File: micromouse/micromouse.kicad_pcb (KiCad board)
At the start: 2 copper layers, 38 parts, among them IC1 STM32F205RET7, J1 B2B-PH-K-S, J2 B2B-PH-K-S, J3 Left Header, J4 Left Header, Q1 SFH_313_FA-3_4, SW1 CK_KMS2xxG, U2 AZ1117IH-3.3TRG1, U3 L293DD, U4 BS170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

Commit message: subsystem grouping
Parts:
- added LED2: LTST-C194TBKT, blue-led:LEDC1608X35N, F.Cu at (92.8, 133.9)
- added LED3: LTST-C194TBKT, blue-led:LEDC1608X35N, F.Cu at (90.8, 64.2)
- added R7: 100 ohm, Resistor_SMD:R_0805_2012Metric, F.Cu at (89.2, 134.1)
- moved J3 116.2 mm to (109.3, 103.2), turned to -90 degrees
- moved C76 114.6 mm to (135.8, 12.5)
- moved C75 111.6 mm to (135.8, 15.3), turned to 180 degrees
- moved J4 110.4 mm to (105.2, 103.2), turned to -90 degrees
- moved U4 108.6 mm to (79.2, 138.4), turned to -90 degrees
- moved C9 106.7 mm to (134.2, 26.8), turned to -90 degrees
- moved C77 105.7 mm to (120.3, 9.45)
- moved C72 103.2 mm to (123.1, 26.8), turned to 180 degrees
- moved C73 99.4 mm to (130.8, 26.6), turned to -90 degrees
- moved R5 99.2 mm to (124.8, 8.06), turned to -90 degrees
- moved C70 98.3 mm to (117.6, 21.2), turned to -90 degrees
- moved LED1 98.2 mm to (79.6, 132.6), turned to 90 degrees
- moved C71 97.5 mm to (114.6, 21.2), turned to -90 degrees
- moved C25 97.0 mm to (123.0, 31.2), turned to 180 degrees
- moved C74 95.1 mm to (117.7, 14.4), turned to 180 degrees
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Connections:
- C5 pad 2: unconnected-(C5-Pad2) -> GND
- R4 pad 2: GND -> Net-(LED3-A)

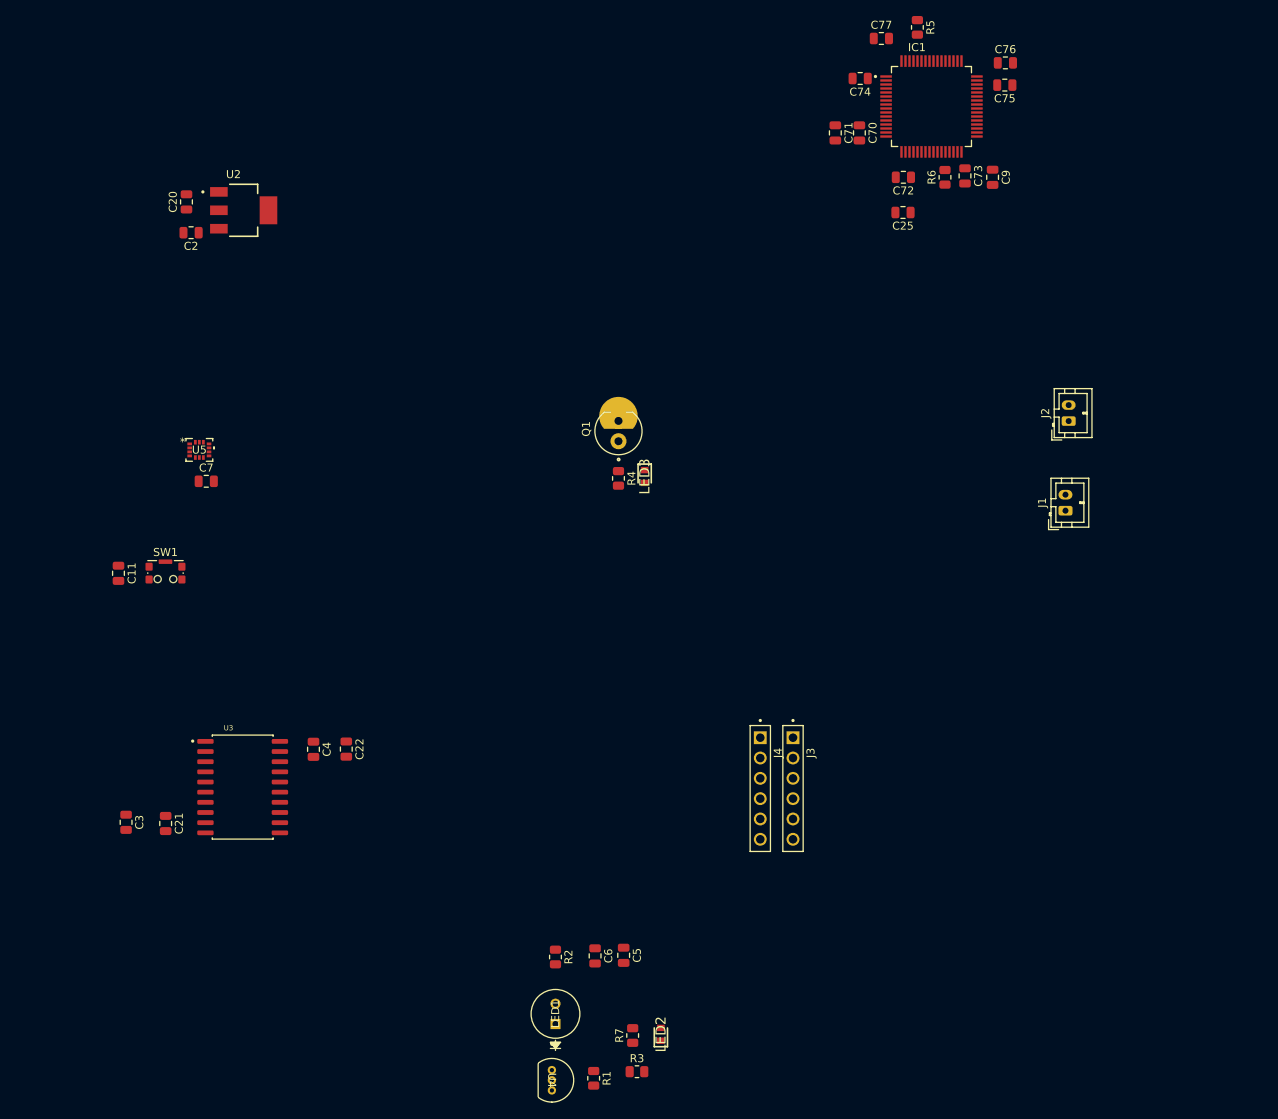
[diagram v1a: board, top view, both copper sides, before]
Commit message: Revision + adding motors
changes to schematic and pcb layout
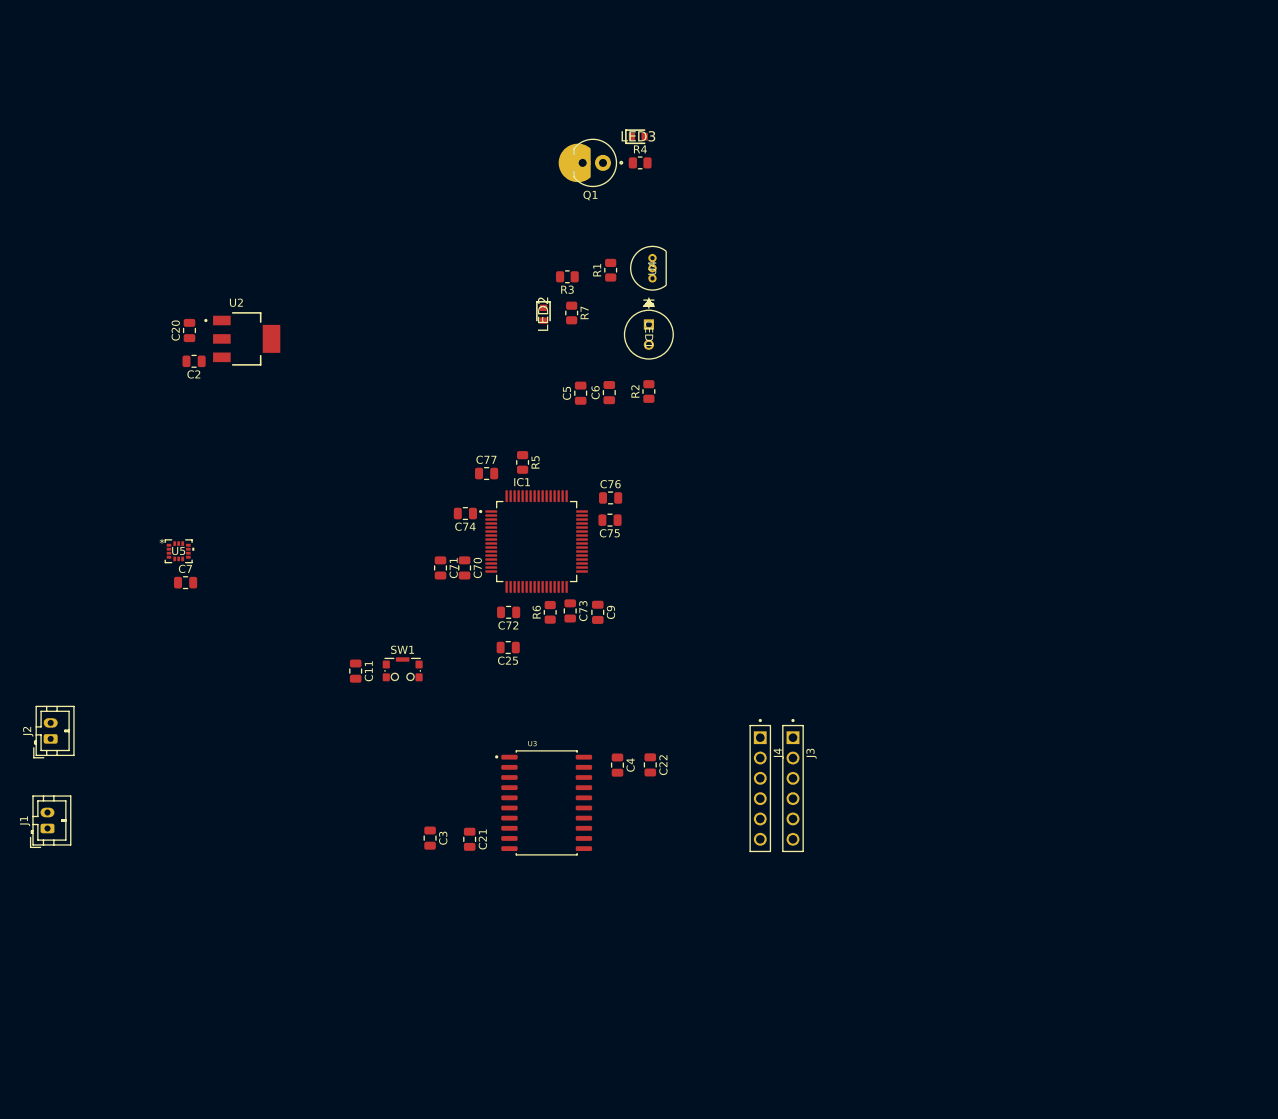
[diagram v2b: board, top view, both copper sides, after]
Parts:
- moved J1 133.3 mm to (16.1, 108.2)
- moved J2 133.3 mm to (16.5, 97.0)
- moved R1 101.0 mm to (86.5, 38.4), turned to 90 degrees
- moved U4 99.8 mm to (91.7, 39.4), turned to 90 degrees
- moved R3 99.7 mm to (81.1, 39.2), turned to 180 degrees
- moved LED2 91.2 mm to (78.1, 43.9), turned to -90 degrees
- moved R7 90.6 mm to (81.6, 43.8), turned to -90 degrees
- moved LED1 88.2 mm to (91.3, 45.2), turned to -90 degrees
- moved C25 73.4 mm to (73.7, 85.6)
- moved C70 73.4 mm to (68.2, 75.6)
- moved C72 73.4 mm to (73.7, 81.2)
- moved C76 73.4 mm to (86.5, 66.9)
- moved C77 73.4 mm to (71.0, 63.8)
- moved C9 73.4 mm to (84.9, 81.2)
- moved R5 73.4 mm to (75.5, 62.4)
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
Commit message: updates to layout
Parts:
- added C1: 4.7 uF, Capacitor_SMD:C_0805_2012Metric, F.Cu at (119.1, 16.7)
- added C10: 4.7 uF, Capacitor_SMD:C_0805_2012Metric, F.Cu at (62.2, 35.7)
- added C12: 0.1 uF, Capacitor_SMD:C_0805_2012Metric, F.Cu at (59.2, 35.7)
- added C13: 4.7 uF, Capacitor_SMD:C_0805_2012Metric, F.Cu at (144.4, 32.5)
- added C14: 0.1 uF, Capacitor_SMD:C_0805_2012Metric, F.Cu at (141.4, 32.5)
- added C8: 0.1 uF, Capacitor_SMD:C_0805_2012Metric, F.Cu at (115.5, 16.8)
- added LED10: LTST-C194TBKT, blue-led:LEDC1608X35N, F.Cu at (147.0, 51.5)
- added LED11: INL-5AMIR15, ir-emitter:LED_INL-5AMIR15_INO, F.Cu at (159.7, 39.4)
- added LED12: LTST-C194TBKT, blue-led:LEDC1608X35N, F.Cu at (145.2, 39.4)
- added LED4: LTST-C194TBKT, blue-led:LEDC1608X35N, F.Cu at (125.5, 41.1)
- added LED5: INL-5AMIR15, ir-emitter:LED_INL-5AMIR15_INO, F.Cu at (132.5, 22.5)
- added LED6: LTST-C194TBKT, blue-led:LEDC1608X35N, F.Cu at (119.7, 25.5)
- added LED7: LTST-C194TBKT, blue-led:LEDC1608X35N, F.Cu at (48.7, 58.6)
- added LED8: INL-5AMIR15, ir-emitter:LED_INL-5AMIR15_INO, F.Cu at (43.9, 40.4)
- added LED9: LTST-C194TBKT, blue-led:LEDC1608X35N, F.Cu at (59.0, 42.4)
- added Motor1: ~, Pololu_Motor:Pololu_Motor, F.Cu at (48.6, 78.6)
- added Motor2: ~, Pololu_Motor:Pololu_Motor, F.Cu at (155.0, 82.2)
- added Q2: SFH_313_FA-3_4, ir reciever:XDCR_SFH_313_FA-3_4, F.Cu at (123.8, 17.5)
- added Q3: SFH_313_FA-3_4, ir reciever:XDCR_SFH_313_FA-3_4, F.Cu at (51.8, 34.6)
- added Q4: SFH_313_FA-3_4, ir reciever:XDCR_SFH_313_FA-3_4, F.Cu at (151.6, 32.7)
- added R10: 47k, Resistor_SMD:R_0805_2012Metric, F.Cu at (133.2, 34.6)
- added R11: 51 ohm, Resistor_SMD:R_0805_2012Metric, F.Cu at (132.3, 14.4)
- added R12: 1.8k, Resistor_SMD:R_0805_2012Metric, F.Cu at (123.9, 25.7)
- added R13: 300 ohm, Resistor_SMD:R_0805_2012Metric, F.Cu at (48.7, 54.7)
- added R14: 100 ohm, Resistor_SMD:R_0805_2012Metric, F.Cu at (45.4, 53.1)
- added R15: 47k, Resistor_SMD:R_0805_2012Metric, F.Cu at (43.0, 53.3)
- added R16: 51 ohm, Resistor_SMD:R_0805_2012Metric, F.Cu at (43.5, 31.5)
- added R17: 1.8k, Resistor_SMD:R_0805_2012Metric, F.Cu at (53.9, 42.5)
- added R18: 300 ohm, Resistor_SMD:R_0805_2012Metric, F.Cu at (147.0, 46.2)
- added R19: 100 ohm, Resistor_SMD:R_0805_2012Metric, F.Cu at (151.1, 46.5)
- added R20: 47k, Resistor_SMD:R_0805_2012Metric, F.Cu at (161.7, 51.8)
- added R21: 51 ohm, Resistor_SMD:R_0805_2012Metric, F.Cu at (151.9, 25.4)
- added R22: 1.8k, Resistor_SMD:R_0805_2012Metric, F.Cu at (149.9, 39.4)
- added R8: 300 ohm, Resistor_SMD:R_0805_2012Metric, F.Cu at (125.3, 36.4)
- added R9: 100 ohm, Resistor_SMD:R_0805_2012Metric, F.Cu at (129.4, 34.8)
- added SW2: EG1218, power-switch:SW_1218_EWI, F.Cu at (106.7, 109.9)
- added U1: BS170, bs170:TO_SA06_ONS, F.Cu at (131.0, 29.7)
- added U6: BS170, bs170:TO_SA06_ONS, F.Cu at (42.0, 46.9)
- added U7: BS170, bs170:TO_SA06_ONS, F.Cu at (158.4, 46.7)
- R7: value 100 ohm -> 300 ohm
- moved J1 94.4 mm to (110.0, 118.8), turned to 180 degrees
- moved J2 85.0 mm to (98.8, 118.4), turned to 180 degrees
- moved C7 84.7 mm to (108.7, 38.8), turned to 180 degrees
- moved U2 81.2 mm to (104.0, 98.3)
- moved C2 81.1 mm to (94.8, 104.0)
- moved U5 80.4 mm to (104.8, 38.3)
- moved C20 78.5 mm to (93.2, 97.3)
- moved C11 43.9 mm to (73.8, 49.1)
- moved SW1 43.9 mm to (79.7, 49.1)
- moved R2 41.9 mm to (72.1, 16.4), turned to -90 degrees
- moved C5 37.9 mm to (91.9, 17.0), turned to -90 degrees
- moved C6 36.8 mm to (88.9, 17.0), turned to -90 degrees
- moved C76 35.9 mm to (113.6, 43.2)
- moved C75 35.9 mm to (113.5, 46.0)
- moved R5 34.5 mm to (99.7, 37.8)
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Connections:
- IC1 pad 10: unconnected-(IC1-PC2-Pad10) -> PC2
- IC1 pad 15: unconnected-(IC1-PA1-Pad15) -> PA1
- IC1 pad 16: unconnected-(IC1-PA2-Pad16) -> PA2
- IC1 pad 20: unconnected-(IC1-PA4-Pad20) -> PA4
- IC1 pad 21: unconnected-(IC1-PA5-Pad21) -> PA5
- IC1 pad 25: unconnected-(IC1-PC5-Pad25) -> PC5
- IC1 pad 58: I2C1_SCL -> SCL
- IC1 pad 59: I2C1_SDA -> SDA
- IC1 pad 9: unconnected-(IC1-PC1-Pad9) -> PC1
- J1 pad 1: VCC -> Net-(J1-Pad1)
- Q1 pad 1: PC5 -> PC1
- R3 pad 1: PC9 -> PC2
- R4 pad 1: PC5 -> PC1
- R7 pad 1: PC9 -> PC2
- SW1 pad SH: unconnected-(SW1-B-PadSH) -> GND
- U5 pad 13: /SCL -> SCL
- U5 pad 14: /SDA -> SDA

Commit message: pcb updates
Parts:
- removed U1, U4, U6, U7: BS170, bs170:TO_SA06_ONS
- added J5: Conn_01x04_Pin, Connector_PinHeader_2.54mm:PinHeader_1x04_P2.54mm_Vertical, F.Cu at (160.7, 61.3)
- added Q5: 2N7002LT1G, new_n_channel_mosfets:SOT95P240X111-3N, F.Cu at (73.0, 29.8)
- added Q6: 2N7002LT1G, new_n_channel_mosfets:SOT95P240X111-3N, F.Cu at (132.3, 28.0)
- added Q7: 2N7002LT1G, new_n_channel_mosfets:SOT95P240X111-3N, F.Cu at (160.6, 46.5)
- added Q8: 2N7002LT1G, new_n_channel_mosfets:SOT95P240X111-3N, F.Cu at (44.1, 47.4)
- moved Motor1 9.03 mm to (48.9, 87.6)
- moved R21 8.94 mm to (158.9, 31.0), turned to -90 degrees
- moved Motor2 8.55 mm to (156.3, 90.6)
- moved C22 4.85 mm to (110.4, 75.9), turned to 90 degrees
- moved C4 4.52 mm to (114.5, 75.8), turned to 90 degrees
- moved R11 2.35 mm to (133.3, 16.5)
- moved C70 1.75 mm to (90.2, 51.9)
- moved C71 1.75 mm to (87.2, 51.9)
- moved C74 1.50 mm to (89.5, 45.3)
- moved R2 1.01 mm to (73.1, 16.5)
- moved Q2 0.91 mm to (123.8, 18.4)
- moved C20 0.90 mm to (94.2, 97.3)
- moved U5 0.66 mm to (104.5, 37.8), turned to 180 degrees
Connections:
- C7 pad 2: +3.3V -> 3V3
- IC1 pad 17: unconnected-(IC1-PA3-Pad17) -> PA3
- IC1 pad 22: unconnected-(IC1-PA6-Pad22) -> PA6
- IC1 pad 23: unconnected-(IC1-PA7-Pad23) -> PA7
- IC1 pad 37: unconnected-(IC1-PC6-Pad37) -> PC6
- IC1 pad 40: unconnected-(IC1-PC9-Pad40) -> PC9
- IC1 pad 41: unconnected-(IC1-PA8-Pad41) -> LENC2
- IC1 pad 42: unconnected-(IC1-PA9-Pad42) -> LENC1
- IC1 pad 56: unconnected-(IC1-PB4-Pad56) -> RENC2
- IC1 pad 57: unconnected-(IC1-PB5-Pad57) -> RENC1
- IC1 pad 62: unconnected-(IC1-PB9-Pad62) -> PB9
- IC1 pad 8: unconnected-(IC1-PC0-Pad8) -> PC0
- J4 pad 3: RENC1 -> RENC2
- Q3 pad 1: PA5 -> PC6
- R13 pad 1: PA6 -> PC0
- R14 pad 1: PA6 -> PC0
- R17 pad 1: PA5 -> PC6
- U3 pad 12: PB8 -> PA3
- U3 pad 2: PB6 -> PA6
- U3 pad 9: PB7 -> PA7
- U5 pad 8: +3.3V -> 3V3
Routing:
- net 3V3: track 0.00 -> 413.2 mm
- net GND: track 0.00 -> 147.8 mm, vias 0 -> 48
- net PC6: track 0.00 -> 76.5 mm, vias 0 -> 2
- net PB9: track 0.00 -> 74.7 mm, vias 0 -> 2
- net PC5: track 0.00 -> 69.3 mm, vias 0 -> 6
- net SWCLK: track 0.00 -> 62.9 mm, vias 0 -> 2
- net SWDIO: track 0.00 -> 61.8 mm, vias 0 -> 2
- net RENC2: track 0.00 -> 59.8 mm, vias 0 -> 2
- net RENC1: track 0.00 -> 58.3 mm, vias 0 -> 2
- net PC0: track 0.00 -> 54.7 mm, vias 0 -> 2
- net PA1: track 0.00 -> 54.7 mm, vias 0 -> 2
- net VCC: track 0.00 -> 49.8 mm
- net PC9: track 0.00 -> 48.0 mm, vias 0 -> 2
- net PA2: track 0.00 -> 43.7 mm, vias 0 -> 2
- net LENC2: track 0.00 -> 41.9 mm, vias 0 -> 4
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- added copper zone on B.Cu, net GND
- added copper zone on F.Cu, net GND
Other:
- board outline added: 128.6 x 114.7 mm

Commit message: changes
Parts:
- Q1, Q2: value SFH_313_FA-3_4 -> ir_reciever
- moved U5 11.6 mm to (106.7, 26.4)
- moved Q1 2.38 mm to (81.9, 16.0), turned to 180 degrees
- moved Q2 2.20 mm to (124.1, 16.2), turned to 0 degrees
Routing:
- net 3V3: track 413.2 -> 431.2 mm
- net SCL: track 6.85 -> 19.2 mm, vias 2 -> 4
- net SDA: track 7.34 -> 19.6 mm, vias 0 -> 2
- net PC1: track 37.8 -> 42.0 mm
- net PA1: track 54.7 -> 58.6 mm

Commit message: updates
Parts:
- moved Motor2 3.65 mm to (159.9, 90.8)
- moved Motor1 1.88 mm to (47.0, 87.8)
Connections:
- J2 pad 2: GND -> MGND
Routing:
- net MGND: track 3.81 -> 64.6 mm, vias 0 -> 2
- net GND: track 147.8 -> 87.0 mm, vias 48 -> 46
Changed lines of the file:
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@@
 	(footprint "Pololu_Motor:Pololu_Motor"
 		(layer "F.Cu")
-		(at 156.275 90.625 -90)
+		(at 159.925 90.75 -90)
 		(property "Reference" "Motor2"
 			(at -8.6 8.2 0)
@@
 	(footprint "Pololu_Motor:Pololu_Motor"
 		(layer "F.Cu")
-		(at 48.925 87.625 90)
+		(at 47.05 87.75 90)
 		(property "Reference" "Motor1"
 			(at -9.8 5.1 90)
@@
 			(layers "*.Cu" "*.Mask")
 			(remove_unused_layers no)
-			(net 1 "GND")
+			(net 5 "MGND")
 			(pinfunction "2")
 			(pintype "passive")
@@
 	)
 	(segment
-		(start 92.205 91.61)
-		(end 87.405 91.61)
-		(width 1)
-		(layer "F.Cu")
-		(net 1)
-	)
-	(segment
 		(start 87.175 53.87403)
 		(end 87.125 53.92403)
@@
 	)
 	(segment
-		(start 81.865 91.46)
-		(end 87.255 91.46)
-		(width 1)
-		(layer "F.Cu")
-		(net 1)
-	)
-	(segment
 		(start 144.45 33.455)
 		(end 143.75 34.155)
@@
 	)
 	(segment
-		(start 92.05 90.075)
-		(end 92.05 91.455)
-		(width 1)
-		(layer "F.Cu")
-		(net 1)
-	)
-	(segment
-		(start 96.75 118.375)
-		(end 96.75 111.9)
-		(width 1)
-		(layer "F.Cu")
-		(net 1)
-	)
-	(segment
 		(start 114.525 43.325)
 		(end 115.65 44.45)
@@
 	)
 	(segment
-		(start 97.1 80.955)
-		(end 97.1 84.765)
-		(width 1)
-		(layer "F.Cu")
-		(net 1)
-	)
-	(segment
 		(start 59.775 42.409089)
 		(end 59.775 41.625)
@@
 	)
 	(segment
-		(start 92.05 91.455)
-		(end 92.205 91.61)
-		(width 1)
-		(layer "F.Cu")
-		(net 1)
-	)
-	(segment
 		(start 46.05 46.425)
 		(end 46.525 45.95)
@@
 	)
 	(segment
-		(start 87.405 91.61)
-		(end 87.255 91.46)
-		(width 1)
-		(layer "F.Cu")
-		(net 1)
-	)
-	(segment
-		(start 96.594 80.955)
-		(end 92.85 84.699)
-		(width 1)
-		(layer "F.Cu")
-		(net 1)
-	)
-	(segment
 		(start 99.65 36.8375)
 		(end 99.1375 36.8375)
@@
 	)
 	(segment
-		(start 97.1 80.955)
-		(end 96.594 80.955)
-		(width 1)
-		(layer "F.Cu")
-		(net 1)
-	)
-	(segment
 		(start 115.45 19.375)
 		(end 115.35 19.475)
@@
 	)
 	(segment
-		(start 96.75 111.9)
-		(end 81.45 96.6)
-		(width 1)
-		(layer "F.Cu")
-		(net 1)
-	)
-	(segment
 		(start 115.45 17.715)
 		(end 115.45 19.375)
@@
 	)
 	(segment
-		(start 81.45 91.875)
-		(end 81.865 91.46)
-		(width 1)
-		(layer "F.Cu")
-		(net 1)
-	)
-	(segment
 		(start 106.69265 24.53235)
 		(end 106.80735 24.41765)
@@
 		(net 1)
 	)
-	(segment
-		(start 81.45 96.6)
-		(end 81.45 91.875)
-		(width 1)
-		(layer "F.Cu")
-		(net 1)
-	)
 	(via
 		(at 60.5 40.9)
@@
 	)
 	(via
-		(at 92.85 84.699)
-		(size 0.6)
-		(drill 0.3)
-		(layers "F.Cu" "B.Cu")
-		(net 1)
-	)
-	(via
 		(at 41.425 55.575)
 		(size 0.6)
@@
 	)
 	(via
-		(at 92.05 90.075)
-		(size 0.6)
-		(drill 0.3)
-		(layers "F.Cu" "B.Cu")
-		(net 1)
-	)
-	(via
 		(at 92.35 64.475)
 		(size 0.6)
@@
 	)
 	(segment
-		(start 92.85 84.699)
-		(end 92.85 89.275)
-		(width 1)
-		(layer "B.Cu")
-		(net 1)
-	)
-	(segment
-		(start 92.85 89.275)
-		(end 92.05 90.075)
-		(width 1)
-		(layer "B.Cu")
-		(net 1)
-	)
-	(segment
 		(start 96.9125 102.8125)
 		(end 95.7 104.025)
@@
 		(net 5)
 	)
+	(segment
+		(start 92.205 91.61)
+		(end 87.405 91.61)
+		(width 1)
+		(layer "F.Cu")
+		(net 5)
+	)
+	(segment
+		(start 81.865 91.46)
+		(end 87.255 91.46)
+		(width 1)
+		(layer "F.Cu")
+		(net 5)
+	)
+	(segment
+		(start 92.05 90.075)
+		(end 92.05 91.455)
+		(width 1)
+		(layer "F.Cu")
+		(net 5)
+	)
+	(segment
+		(start 96.75 118.375)
+		(end 96.75 111.9)
+		(width 1)
+		(layer "F.Cu")
+		(net 5)
+	)
+	(segment
+		(start 97.1 80.955)
+		(end 97.1 84.765)
+		(width 1)
+		(layer "F.Cu")
+		(net 5)
+	)
+	(segment
+		(start 92.05 91.455)
+		(end 92.205 91.61)
+		(width 1)
+		(layer "F.Cu")
+		(net 5)
+	)
+	(segment
+		(start 87.405 91.61)
+		(end 87.255 91.46)
+		(width 1)
+		(layer "F.Cu")
+		(net 5)
+	)
+	(segment
+		(start 96.594 80.955)
+		(end 92.85 84.699)
+		(width 1)
+		(layer "F.Cu")
+		(net 5)
+	)
+	(segment
+		(start 97.1 80.955)
+		(end 96.594 80.955)
+		(width 1)
+		(layer "F.Cu")
+		(net 5)
+	)
+	(segment
+		(start 96.75 111.9)
+		(end 81.45 96.6)
+		(width 1)
+		(layer "F.Cu")
+		(net 5)
+	)
+	(segment
+		(start 81.45 91.875)
+		(end 81.865 91.46)
+		(width 1)
+		(layer "F.Cu")
+		(net 5)
+	)
+	(segment
+		(start 81.45 96.6)
+		(end 81.45 91.875)
+		(width 1)
+		(layer "F.Cu")
+		(net 5)
+	)
+	(via
+		(at 92.85 84.699)
+		(size 0.6)
+		(drill 0.3)
+		(layers "F.Cu" "B.Cu")
+		(free yes)
+		(net 5)
+	)
+	(via
+		(at 92.05 90.075)
+		(size 0.6)
+		(drill 0.3)
+		(layers "F.Cu" "B.Cu")
+		(free yes)
+		(net 5)
+	)
+	(segment
+		(start 92.85 84.699)
+		(end 92.85 89.275)
+		(width 1)
+		(layer "B.Cu")
+		(net 5)
+	)
+	(segment
+		(start 92.85 89.275)
+		(end 92.05 90.075)
+		(width 1)
+		(layer "B.Cu")
+		(net 5)
+	)
